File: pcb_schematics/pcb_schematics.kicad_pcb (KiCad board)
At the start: 2 copper layers, 100 x 100 mm, 52 parts, among them J1 CUE_SJ1-352XNG, J2 Conn_01x01_Pin, J3 Conn_01x05, J4 Conn_01x05, J5 Conn_01x05, SW1 SW_Push, U1 RPi_Pico_TH, U2 RDA5807M_Module, U3 LM386, U4 LM386

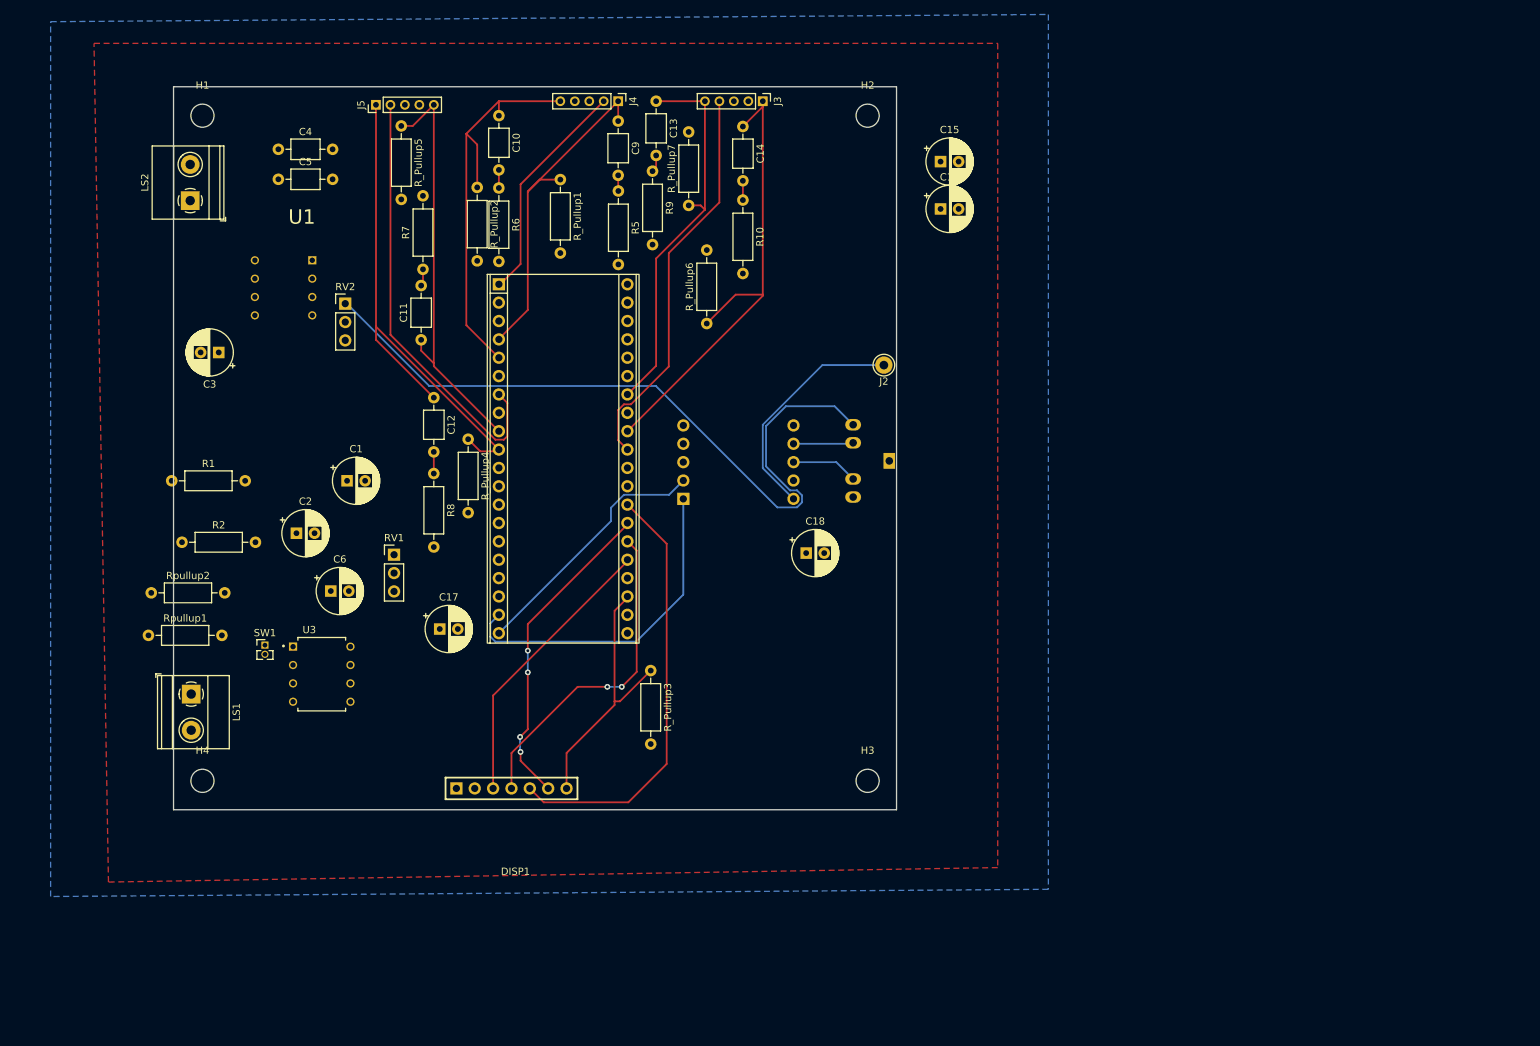
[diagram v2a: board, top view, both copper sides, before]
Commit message: compeltes PCB
Only the DRC has a couple errors
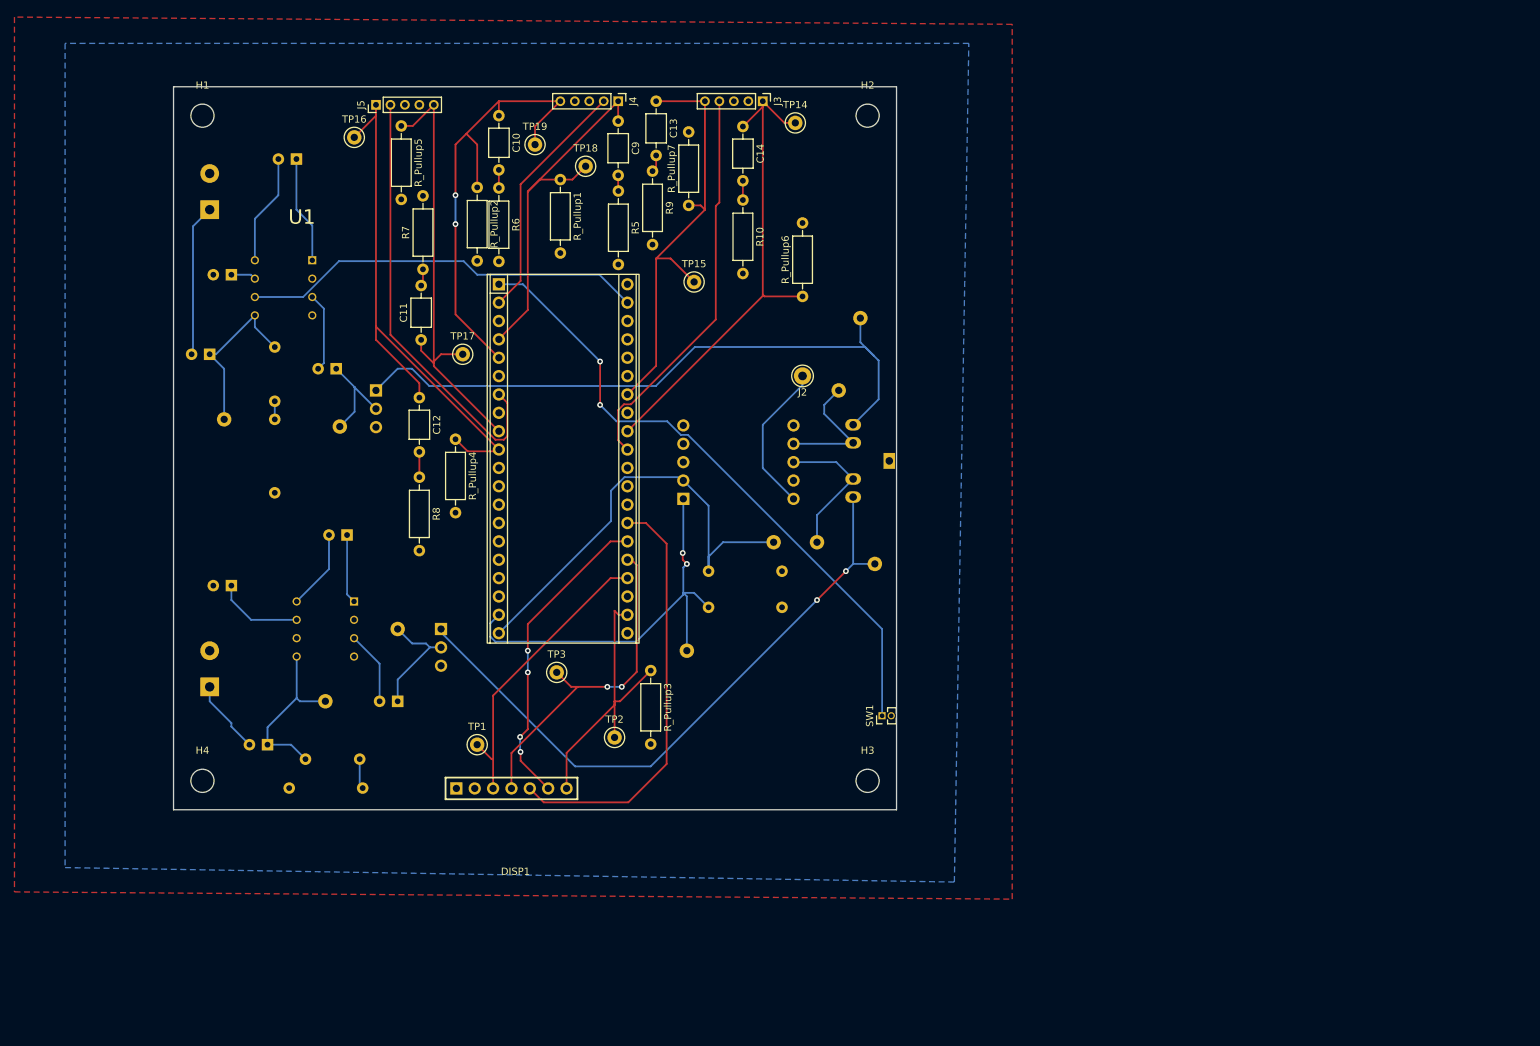
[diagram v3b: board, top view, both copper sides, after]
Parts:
- added TP1: TestPoint, TestPoint:TestPoint_Keystone_5000-5004_Miniature, F.Cu at (87.0, 116.0)
- added TP10: TestPoint, TestPoint:TestPoint_Keystone_5000-5004_Miniature, B.Cu at (134.0, 88.0)
- added TP11: TestPoint, TestPoint:TestPoint_Keystone_5000-5004_Miniature, B.Cu at (137.0, 67.0)
- added TP12: TestPoint, TestPoint:TestPoint_Keystone_5000-5004_Miniature, B.Cu at (140.0, 57.0)
- added TP13: TestPoint, TestPoint:TestPoint_Keystone_5000-5004_Miniature, B.Cu at (142.0, 91.0)
- added TP14: TestPoint, TestPoint:TestPoint_Keystone_5000-5004_Miniature, F.Cu at (131.0, 30.0)
- added TP15: TestPoint, TestPoint:TestPoint_Keystone_5000-5004_Miniature, F.Cu at (117.0, 52.0)
- added TP16: TestPoint, TestPoint:TestPoint_Keystone_5000-5004_Miniature, F.Cu at (70.0, 32.0)
- added TP17: TestPoint, TestPoint:TestPoint_Keystone_5000-5004_Miniature, F.Cu at (85.0, 62.0)
- added TP18: TestPoint, TestPoint:TestPoint_Keystone_5000-5004_Miniature, F.Cu at (102.0, 36.0)
- added TP19: TestPoint, TestPoint:TestPoint_Keystone_5000-5004_Miniature, F.Cu at (95.0, 33.0)
- added TP2: TestPoint, TestPoint:TestPoint_Keystone_5000-5004_Miniature, F.Cu at (106.0, 115.0)
- added TP3: TestPoint, TestPoint:TestPoint_Keystone_5000-5004_Miniature, F.Cu at (98.0, 106.0)
- added TP4: TestPoint, TestPoint:TestPoint_Keystone_5000-5004_Miniature, B.Cu at (116.0, 103.0)
- added TP5: TestPoint, TestPoint:TestPoint_Keystone_5000-5004_Miniature, B.Cu at (128.0, 88.0)
- added TP6: TestPoint, TestPoint:TestPoint_Keystone_5000-5004_Miniature, B.Cu at (68.0, 72.0)
- added TP7: TestPoint, TestPoint:TestPoint_Keystone_5000-5004_Miniature, B.Cu at (76.0, 100.0)
- added TP8: TestPoint, TestPoint:TestPoint_Keystone_5000-5004_Miniature, B.Cu at (66.0, 110.0)
- added TP9: TestPoint, TestPoint:TestPoint_Keystone_5000-5004_Miniature, B.Cu at (52.0, 71.0)
- C1, C15, C16, C17, C18, C2, C3, C4, C5, C6, LS1, LS2, R1, R2, RV1, RV2, Rpullup1, Rpullup2, U3: moved to B.Cu
- moved C15 105.9 mm to (76.0, 110.0), turned to 180 degrees
- moved C18 89.1 mm to (62.0, 35.0), turned to 180 degrees
- moved C16 86.5 mm to (67.5, 64.0), turned to 180 degrees
- moved SW1 85.9 mm to (143.0, 112.0), turned to 90 degrees
- moved C5 80.3 mm to (63.2, 118.0)
- moved Rpullup1 78.0 mm to (119.0, 92.0)
- moved Rpullup2 77.1 mm to (119.0, 97.0)
- moved R2 42.2 mm to (71.2, 122.0), turned to 180 degrees
- moved C2 36.9 mm to (53.0, 51.0), turned to 180 degrees
- moved C4 27.4 mm to (59.0, 61.0), turned to -90 degrees
- moved C6 23.0 mm to (58.0, 116.0), turned to 180 degrees
- moved C1 21.6 mm to (53.0, 94.0), turned to 180 degrees
- moved C17 18.3 mm to (69.0, 87.0), turned to 180 degrees
- moved R1 16.6 mm to (59.0, 71.0), turned to -90 degrees
- moved R_Pullup6 13.8 mm to (132.0, 54.0)
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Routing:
- net /LSpeaker: track 0.00 -> 89.0 mm, vias 0 -> 2
- net /SW1: track 0.00 -> 88.3 mm, vias 0 -> 2
- net 5V: track 0.00 -> 56.0 mm
- net /I2CSCK: track 35.3 -> 62.9 mm
- net Net-(C5-Pad1): track 0.00 -> 24.1 mm
- net Net-(C3-Pad1): track 0.00 -> 23.8 mm
- net Net-(C3-Pad2): track 0.00 -> 21.0 mm
- net Net-(C15-Pad1): track 0.00 -> 17.1 mm
- net Net-(C18-Pad2): track 0.00 -> 15.3 mm
- net Net-(C18-Pad1): track 0.00 -> 14.9 mm
- net Net-(C16-Pad1): track 0.00 -> 14.1 mm
- net /I2CTX: track 46.4 -> 59.6 mm, vias 0 -> 2
- net Net-(U3-BYPASS): track 0.00 -> 12.2 mm
- net /RSpeaker: track 102.6 -> 91.0 mm
- net Net-(J2-Pin_1): track 32.2 -> 21.0 mm
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- added copper zone on B.Cu, net /3V3
- added copper zone on F.Cu, net GND
- removed copper zone on F.Cu, net /3V3
- removed copper zone on B.Cu, net GND
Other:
- board text added: "Antenna"
- board text added: "Clock-Radio 29-06-25 Animish Murthy, Krishna Gupta 007, MI6"

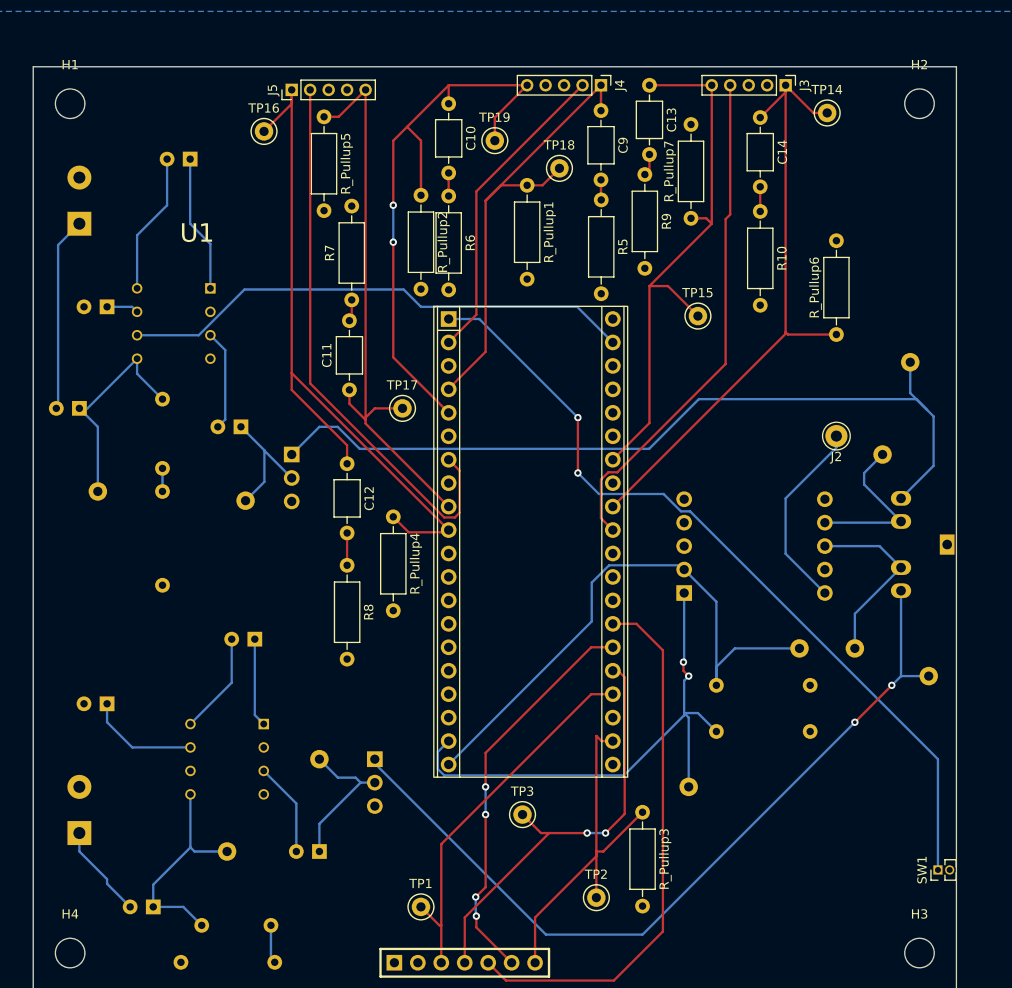
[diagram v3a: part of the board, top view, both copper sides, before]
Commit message: Fixes errors in DRC
Adds SMD capacitors too
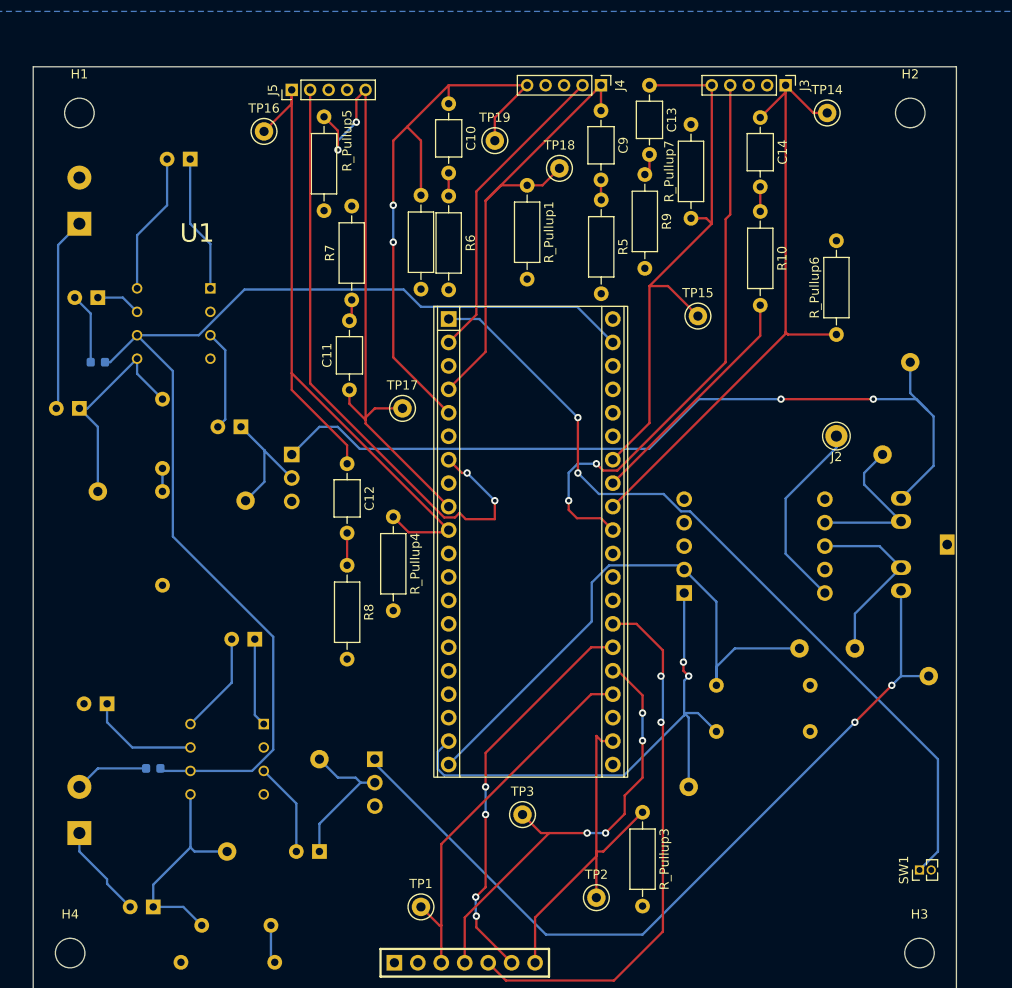
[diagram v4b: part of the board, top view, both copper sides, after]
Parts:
- added C7: 0.1 µF, Capacitor_SMD:C_0603_1608Metric, B.Cu at (52.0, 57.0)
- added C8: 0.1 µF, Capacitor_SMD:C_0603_1608Metric, B.Cu at (58.0, 101.0)
- J1: value CUE_SJ1-352XNG -> Jack
- moved SW1 2.00 mm to (141.0, 112.0)
- moved C2 1.41 mm to (52.0, 50.0)
- moved H1 1.41 mm to (50.0, 30.0)
- moved H2 1.41 mm to (140.0, 30.0)
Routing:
- net 5V: track 56.0 -> 124.9 mm
- net GND: track 0.00 -> 41.7 mm
- net /SW3: track 55.1 -> 62.5 mm, vias 0 -> 2
- net /SW4: track 60.4 -> 67.1 mm, vias 0 -> 2
- net /ROT2A: track 63.0 -> 69.2 mm, vias 0 -> 2
- net /SDA: track 46.4 -> 48.0 mm, vias 2 -> 4
- net Net-(U4-BYPASS): track 3.47 -> 4.89 mm
- net /SW1: track 88.3 -> 89.1 mm
- net /RES: track 59.0 -> 59.3 mm, vias 0 -> 2
- net /RSpeaker: vias 0 -> 2

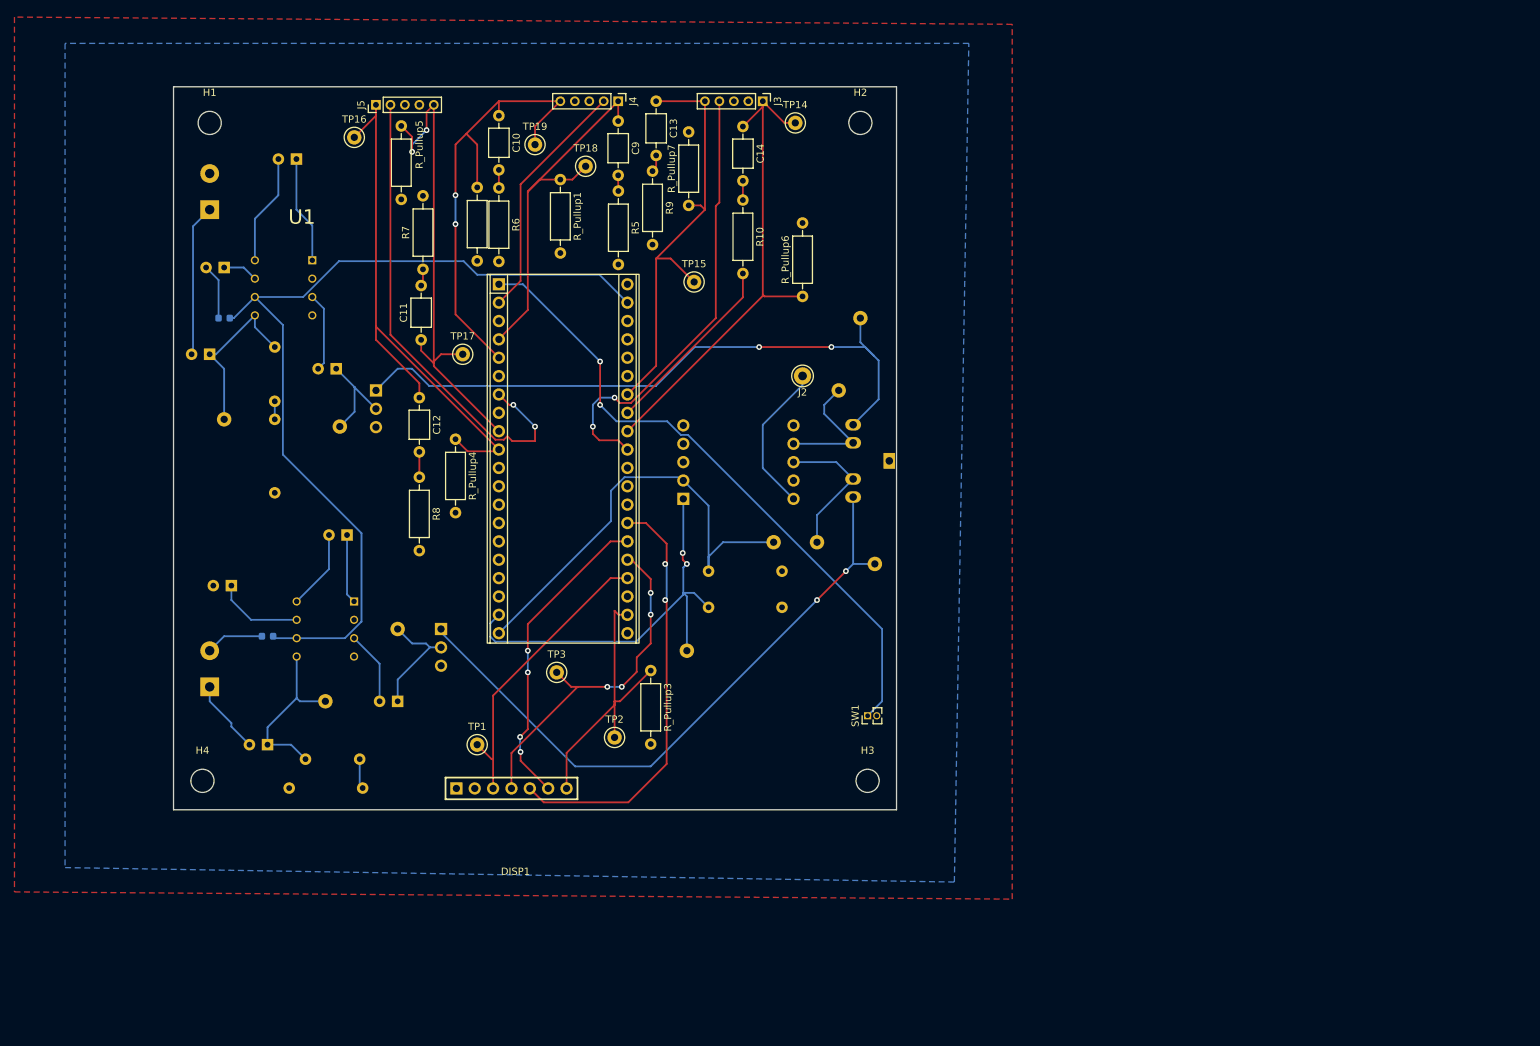
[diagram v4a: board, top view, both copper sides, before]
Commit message: Runs DRC and ERC again
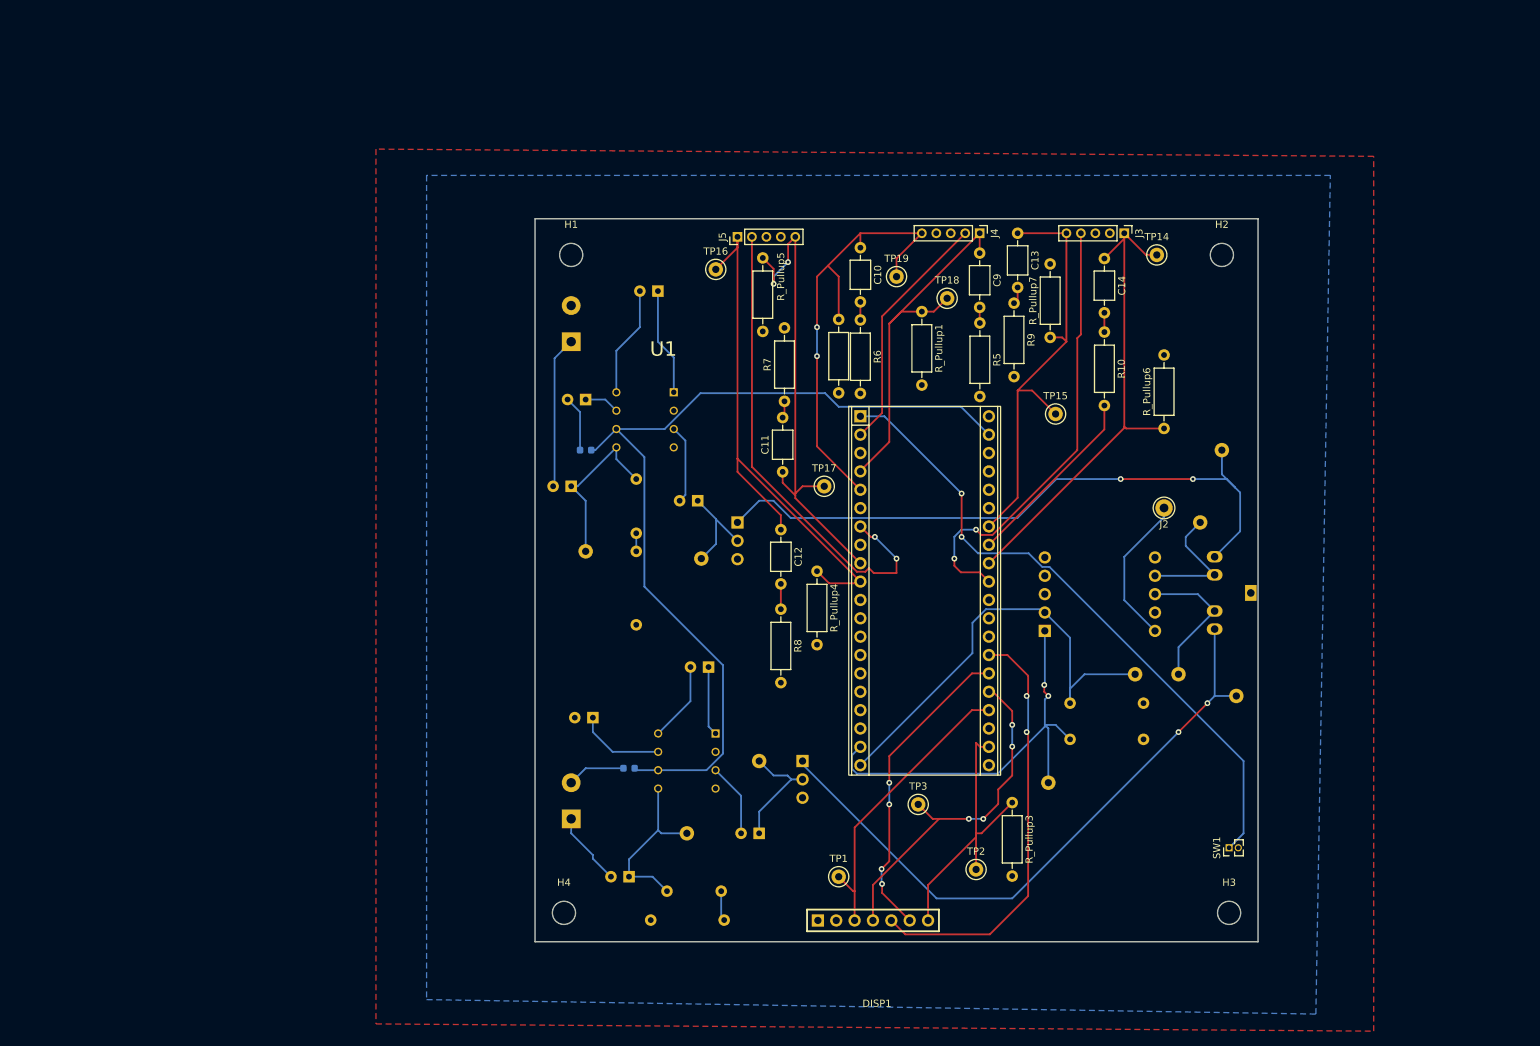
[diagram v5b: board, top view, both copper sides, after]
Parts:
- moved C1 53.2 mm to (103.0, 112.3)
- moved C10 53.2 mm to (140.0, 47.3)
- moved C11 53.2 mm to (129.2, 78.3)
- moved C12 53.2 mm to (129.0, 86.3)
- moved C13 53.2 mm to (161.8, 45.3)
- moved C14 53.2 mm to (173.8, 48.8)
- moved C15 53.2 mm to (126.0, 128.3)
- moved C16 53.2 mm to (117.5, 82.3)
- moved C17 53.2 mm to (119.0, 105.3)
- moved C18 53.2 mm to (112.0, 53.3)
- moved C2 53.2 mm to (102.0, 68.3)
- moved C3 53.2 mm to (100.0, 80.3)
- moved C4 53.2 mm to (109.0, 79.3)
- moved C5 53.2 mm to (113.2, 136.3)
- moved C6 53.2 mm to (108.0, 134.3)
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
